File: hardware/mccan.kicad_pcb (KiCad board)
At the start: 4 copper layers, 140 x 100 mm, 237 parts, among them J1 PWR pigtail -> SS1.5 3w, J2 Prog/UART, J3 FL pigtail -> SS1.0 key A / b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, J4 FR pigtail -> SS1.0 key B / g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, J5 RL pigtail -> SS1.0 key C / b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, J6 RR pigtail -> SS1.0 key D / n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, J7 DENALI pigtail -> SS1.5 3w, J8 CAN pigtail -> SS1.0 2w, Q10 IPT008N06NM5LF, Q11 IPT008N06NM5LF, Q12 MMBT3904, Q2 MMBT3904, Q3 MMBT3904, Q4 NX5020UNBKS, Q5 NX5020UNBKS, Q6 NX5020UNBKS, Q7 NX5020UNBKS, Q8 NX5020UNBKS, Q9 NX5020UNBKS, SW1 BOOT, SW2 EN/RESET, U1 LM5164DDA, U10 LTC4380HMS-2, U2 LM5164DDA, U3 LM51571-Q1, U5 ESP32-WROOM-32E-N8, U6 TJA1042T/3, U7 PCA9685PW/Q900, U8 ADG706, U9 BTS7008-2EPA

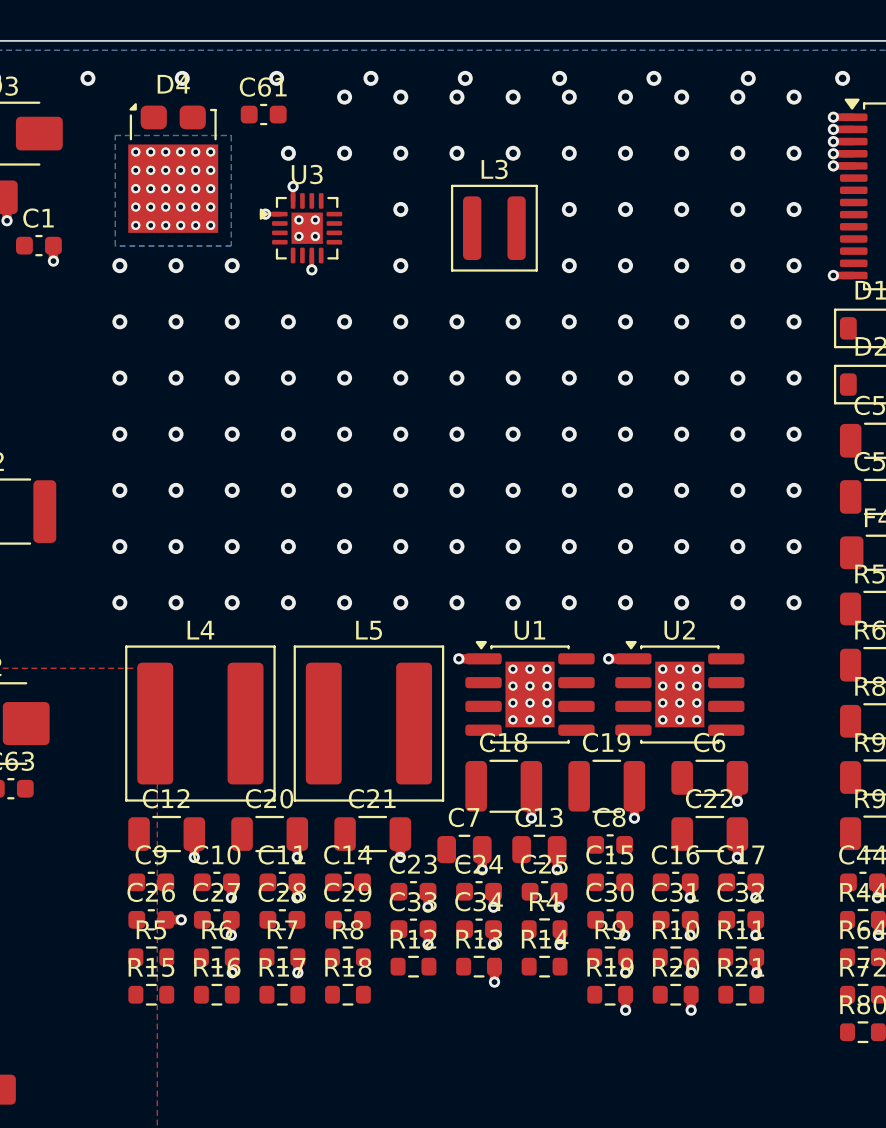
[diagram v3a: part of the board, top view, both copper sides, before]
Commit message: hw(pcb): put the boost's own components next to the boost
U3's entire support network was ~35 mm away, in the `rails` region.  Not because anyone put
it there, but because nobody put it anywhere: layout_pcb.BLOCK pinned only U3, L3, D4 and
C61 to the `boost` region, so every passive fell through to SHEET_REGION and followed its
schematic sheet, which is `rails`.  The region's own comment already said what was meant --
"U3, L3, D4, C61 and their passives" -- and the passives were simply never listed.

What that produced: COMP 35 mm from pin 8, SS 33 mm from pin 10, the FB divider 37 mm from
pin 9, VCC and BIAS with no local bypass at all, and both the input capacitors (C18/C19) and
the output capacitors (C20/C21/C22) roughly 35 mm from the parts they decouple.  COMP is the
error amplifier's output and the highest-impedance node in the converter; a 35 mm run to its
compensation network, past the switch node, is how a boost oscillates.  The switch node
itself spanned 17 mm, which makes a nonsense of "minimise the switch-node loop".

The cluster is now laid out around U3's pinout rather than as a row, because the pinout is
what decides where each network can go: SW on the right and top edges (12, 13, 14), VCC and
BIAS on the left (2, 3), RT/EN/COMP on the bottom (5, 6, 8), FB/SS/MODE on the right
(9, 10, 11).  So the power parts go above and right, the bias network left, the control
network below and right, and nothing has to cross the switch node.

  switch node   17.0 mm -> 5.1 mm span; D4 anode 2.3 mm from U3 pin 14
  FB            37 mm -> a 3.4 mm cluster, R12/C61/R13 in a column with FB facing U3
  COMP          35 mm -> 1.9 mm to R14
  VCC / BIAS    no local bypass -> 2.1 mm and 1.8 mm
  output caps   ~35 mm -> a 1206 column 1.1 mm off D4's cathode tab
  MODE / SS     35 mm -> 5-7 mm; a static level and a slow ramp, so they take the long stubs

VBAT does not need a track to reach L3: In2.Cu is a VBAT plane end to end since ae9319e, so
L3 pad 1 and C18/C19 each re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
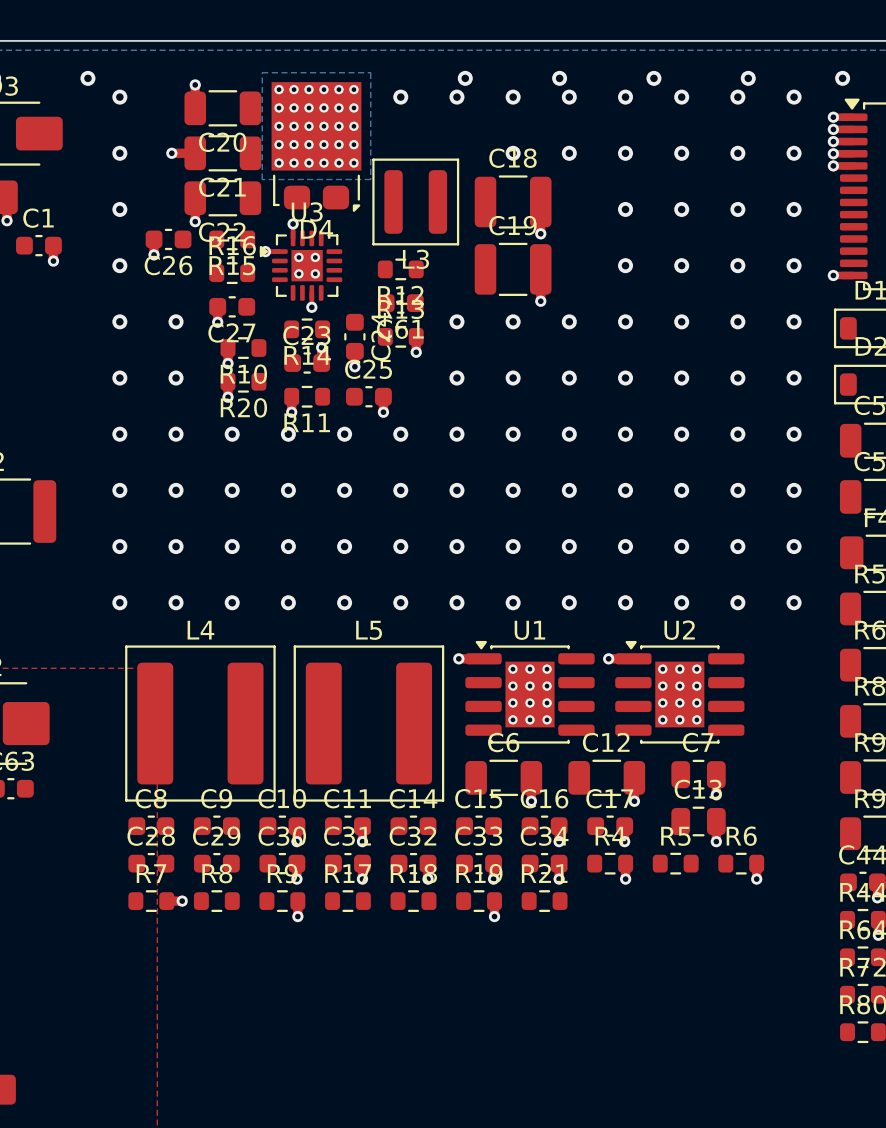
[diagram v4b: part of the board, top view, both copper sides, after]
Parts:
- moved C22 42.8 mm to (69.5, 28.4), turned to 180 degrees
- moved R15 40.6 mm to (70.0, 30.6), turned to 180 degrees
- moved R20 40.0 mm to (70.6, 38.2), turned to 180 degrees
- moved R10 39.9 mm to (70.6, 36.4), turned to 180 degrees
- moved C20 38.8 mm to (69.5, 23.6), turned to 180 degrees
- moved R16 38.5 mm to (70.0, 32.4)
- moved R11 37.9 mm to (74.0, 39.0), turned to 180 degrees
- moved R12 37.2 mm to (79.0, 32.2), turned to 180 degrees
- moved C21 37.2 mm to (69.5, 26.0), turned to 180 degrees
- moved C26 36.3 mm to (66.6, 30.6), turned to 180 degrees
- moved R14 36.3 mm to (74.0, 35.4), turned to 180 degrees
- moved R13 33.9 mm to (79.0, 35.8)
- moved C27 32.7 mm to (70.0, 34.2), turned to 180 degrees
- moved C18 31.2 mm to (85.0, 28.6)
- moved C24 30.4 mm to (76.5, 35.8), turned to 270 degrees
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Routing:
- net GND: vias 331 -> 312

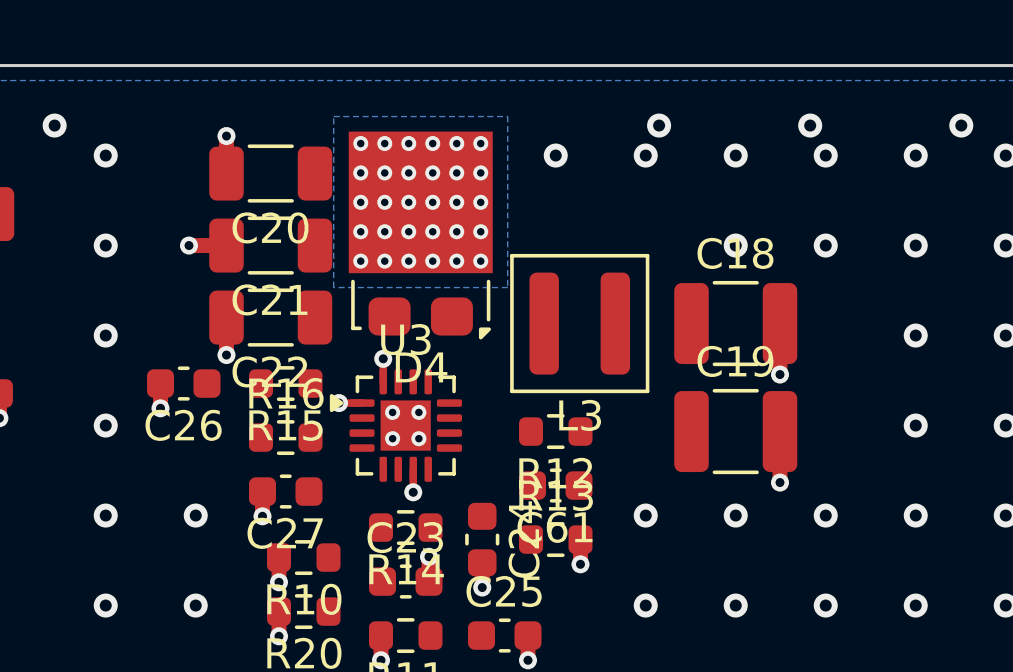
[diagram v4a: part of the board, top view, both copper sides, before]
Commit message: hw(pcb): Task 9 step 1 - route the boost power stage
Adds a route mechanism and uses it for the commutation loop.

layout_pcb.ROUTES is (net, layer, width, [points]) and ROUTE_VIAS is (net, x, y, size,
drill); gen_pcb.routes() emits them and checks two things that are easy to get wrong by hand
and invisible afterwards: that every polyline END lands on copper of its own net, and that
nothing sits closer to a foreign pad than the wider of the two net classes allows.  Both
tests work on COPPER OVERLAP, not on centrelines, because that is what KiCad's connectivity
actually uses -- a 0.75 mm track whose centreline runs between two 0.25 mm QFN pads still
connects to both, and requiring the centreline to hit a pad would rule out the only geometry
that works on a 0.5 mm pitch part.  Nets are named by their last path component, so the
table says "SW_BOOST" and not "/rails/SW_BOOST".

Neither check replaces DRC.  They exist because a coordinate typo produces a board that
looks routed and that DRC can only describe as "unconnected item", somewhere, in a list of
hundreds.  The clearance check earned its keep immediately: the SW track's end cap overlapped
U3's exposed ground paddle, which I had not accounted for because I was thinking about the
endpoint rather than the 0.375 mm of copper past it.

What is routed:

  SW_BOOST   U3 pins 13/14 straight up into D4's anode on one 0.75 mm track, L3 joining from
             the east along y 29.70, and pin 12 tied in at 0.3 mm.  D4 moved 0.8 mm east
             (and L3 and C18/C19 with it) so that D4's anode pad sits directly above pins 13
             and 14: a 0.75 mm track centred between them at x 74.5 overlaps both and still
             clears pin 15 by 0.25 mm.  You cannot bring 0.75 mm of copper into one pin of a
             0.5 mm pitch QFN, but you can bring it into two adjacent pins of the same net,
             and the switch node is worth arranging the placement around to get it.
  +24V       a 1.0 mm column picking up a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
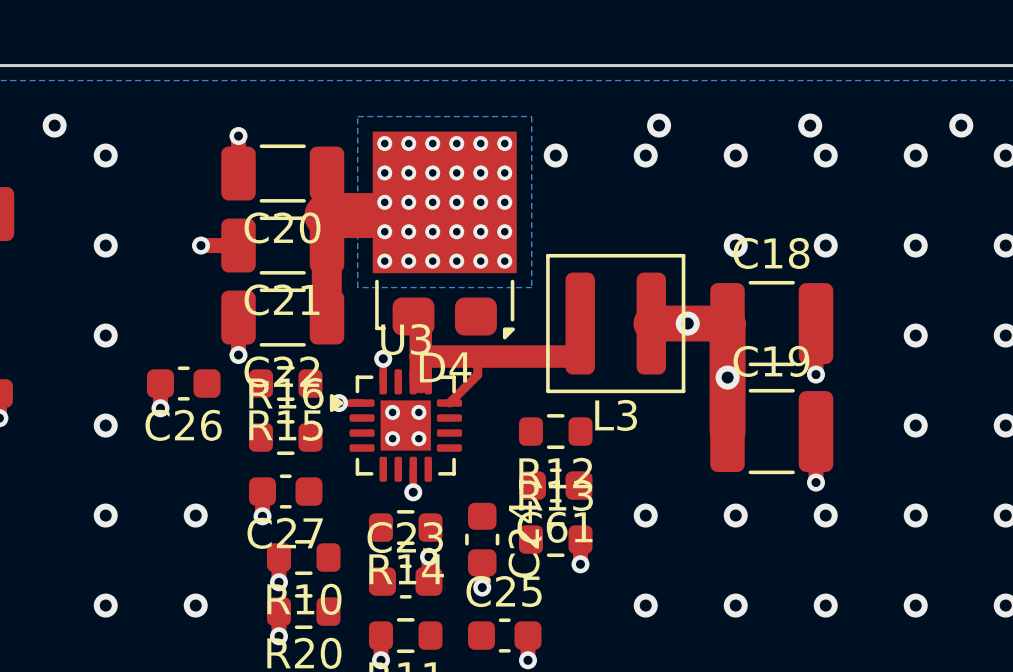
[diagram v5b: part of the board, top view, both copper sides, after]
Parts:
- moved C18 1.20 mm to (86.2, 28.6)
- moved C19 1.20 mm to (86.2, 32.2)
- moved L3 1.20 mm to (81.0, 28.6)
- moved D4 0.80 mm to (75.3, 25.6)
- moved C20 0.40 mm to (69.9, 23.6)
- moved C21 0.40 mm to (69.9, 26.0)
- moved C22 0.40 mm to (69.9, 28.4)
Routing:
- net /rails/SW_BOOST: track 0.00 -> 9.43 mm
- net /+24V: track 0.00 -> 7.03 mm
- net /VBAT: track 0.00 -> 6.14 mm, vias 15 -> 17
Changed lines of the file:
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@@
 	(footprint "Capacitor_SMD:C_1210_3225Metric"
 		(layer "F.Cu")
-		(at 85 28.6)
+		(at 86.2 28.6)
 		(descr "Capacitor SMD 1210 (3225 Metric), square (rectangular) end terminal, IPC-7351 nominal, (Body size source: IPC-SM-782 page 76, https://www.pcb-3d.com/wordpress/wp-content/uploads/ipc-sm-782a_amendment_1_and_2.pdf)")
 		(tags "capacitor")
@@
 	(footprint "Capacitor_SMD:C_1210_3225Metric"
 		(layer "F.Cu")
-		(at 85 32.2)
+		(at 86.2 32.2)
 		(descr "Capacitor SMD 1210 (3225 Metric), square (rectangular) end terminal, IPC-7351 nominal, (Body size source: IPC-SM-782 page 76, https://www.pcb-3d.com/wordpress/wp-content/uploads/ipc-sm-782a_amendment_1_and_2.pdf)")
 		(tags "capacitor")
@@
 	(footprint "Capacitor_SMD:C_1206_3216Metric"
 		(layer "F.Cu")
-		(at 69.5 23.6 180)
+		(at 69.9 23.6 180)
 		(descr "Capacitor SMD 1206 (3216 Metric), square (rectangular) end terminal, IPC-7351 nominal, (Body size source: IPC-SM-782 page 76, https://www.pcb-3d.com/wordpress/wp-content/uploads/ipc-sm-782a_amendment_1_and_2.pdf)")
 		(tags "capacitor")
@@
 	(footprint "Capacitor_SMD:C_1206_3216Metric"
 		(layer "F.Cu")
-		(at 69.5 26 180)
+		(at 69.9 26 180)
 		(descr "Capacitor SMD 1206 (3216 Metric), square (rectangular) end terminal, IPC-7351 nominal, (Body size source: IPC-SM-782 page 76, https://www.pcb-3d.com/wordpress/wp-content/uploads/ipc-sm-782a_amendment_1_and_2.pdf)")
 		(tags "capacitor")
@@
 	(footprint "Capacitor_SMD:C_1206_3216Metric"
 		(layer "F.Cu")
-		(at 69.5 28.4 180)
+		(at 69.9 28.4 180)
 		(descr "Capacitor SMD 1206 (3216 Metric), square (rectangular) end terminal, IPC-7351 nominal, (Body size source: IPC-SM-782 page 76, https://www.pcb-3d.com/wordpress/wp-content/uploads/ipc-sm-782a_amendment_1_and_2.pdf)")
 		(tags "capacitor")
@@
 	(footprint "Package_TO_SOT_SMD:TO-277A"
 		(layer "F.Cu")
-		(at 74.5 25.6 180)
+		(at 75.3 25.6 180)
 		(descr "Thermal enhanced ultra thin SMD package; 3 leads; body: 4.3x6.1x0.43mm, https://www.vishay.com/docs/95570/to-277asmpc.pdf")
 		(tags "TO-277A SMPC")
@@
 	(footprint "Inductor_SMD:L_Coilcraft_XAL4030-XXX"
 		(layer "F.Cu")
-		(at 79.8 28.6 180)
+		(at 81 28.6 180)
 		(descr "Inductor, Coilcraft, XAL4030-XXX, 4.3x4.3x3.1mm, (https://www.coilcraft.com/getmedia/6adcb47d-8b55-416c-976e-1e22e0d2848c/xal4000.pdf)")
 		(tags "xal")
@@
 	)
 	(via
-		(at 76.5 26.52)
+		(at 77.3 26.52)
 		(size 0.5)
 		(drill 0.25)
@@
 	)
 	(via
-		(at 76.5 25.54)
+		(at 77.3 25.54)
 		(size 0.5)
 		(drill 0.25)
@@
 	)
 	(via
-		(at 76.5 24.56)
+		(at 77.3 24.56)
 		(size 0.5)
 		(drill 0.25)
@@
 	)
 	(via
-		(at 76.5 23.58)
+		(at 77.3 23.58)
 		(size 0.5)
 		(drill 0.25)
@@
 	)
 	(via
-		(at 76.5 22.6)
+		(at 77.3 22.6)
 		(size 0.5)
 		(drill 0.25)
@@
 	)
 	(via
-		(at 75.7 26.52)
+		(at 76.5 26.52)
 		(size 0.5)
 		(drill 0.25)
@@
 	)
 	(via
-		(at 75.7 25.54)
+		(at 76.5 25.54)
 		(size 0.5)
 		(drill 0.25)
@@
 	)
 	(via
-		(at 75.7 24.56)
+		(at 76.5 24.56)
 		(size 0.5)
 		(drill 0.25)
@@
 	)
 	(via
-		(at 75.7 23.58)
+		(at 76.5 23.58)
 		(size 0.5)
 		(drill 0.25)
@@
 	)
 	(via
-		(at 75.7 22.6)
+		(at 76.5 22.6)
 		(size 0.5)
 		(drill 0.25)
@@
 	)
 	(via
-		(at 74.9 26.52)
+		(at 75.7 26.52)
 		(size 0.5)
 		(drill 0.25)
@@
 	)
 	(via
-		(at 74.9 25.54)
+		(at 75.7 25.54)
 		(size 0.5)
 		(drill 0.25)
@@
 	)
 	(via
-		(at 74.9 24.56)
+		(at 75.7 24.56)
 		(size 0.5)
 		(drill 0.25)
@@
 	)
 	(via
-		(at 74.9 23.58)
+		(at 75.7 23.58)
 		(size 0.5)
 		(drill 0.25)
@@
 	)
 	(via
-		(at 74.9 22.6)
+		(at 75.7 22.6)
 		(size 0.5)
 		(drill 0.25)
@@
 	)
 	(via
-		(at 74.1 26.52)
+		(at 74.9 26.52)
 		(size 0.5)
 		(drill 0.25)
@@
 	)
 	(via
-		(at 74.1 25.54)
+		(at 74.9 25.54)
 		(size 0.5)
 		(drill 0.25)
@@
 	)
 	(via
-		(at 74.1 24.56)
+		(at 74.9 24.56)
 		(size 0.5)
 		(drill 0.25)
@@
 	)
 	(via
-		(at 74.1 23.58)
+		(at 74.9 23.58)
 		(size 0.5)
 		(drill 0.25)
@@
 	)
 	(via
-		(at 74.1 22.6)
+		(at 74.9 22.6)
 		(size 0.5)
 		(drill 0.25)
@@
 	)
 	(via
-		(at 73.3 26.52)
+		(at 74.1 26.52)
 		(size 0.5)
 		(drill 0.25)
@@
 	)
 	(via
-		(at 73.3 25.54)
+		(at 74.1 25.54)
 		(size 0.5)
 		(drill 0.25)
@@
 	)
 	(via
-		(at 73.3 24.56)
+		(at 74.1 24.56)
 		(size 0.5)
 		(drill 0.25)
@@
 	)
 	(via
-		(at 73.3 23.58)
+		(at 74.1 23.58)
 		(size 0.5)
 		(drill 0.25)
@@
 	)
 	(via
-		(at 73.3 22.6)
+		(at 74.1 22.6)
 		(size 0.5)
 		(drill 0.25)
@@
 	)
 	(via
-		(at 72.5 26.52)
+		(at 73.3 26.52)
 		(size 0.5)
 		(drill 0.25)
@@
 	)
 	(via
-		(at 72.5 25.54)
+		(at 73.3 25.54)
 		(size 0.5)
 		(drill 0.25)
@@
 	)
 	(via
-		(at 72.5 24.56)
+		(at 73.3 24.56)
 		(size 0.5)
 		(drill 0.25)
@@
 	)
 	(via
-		(at 72.5 23.58)
+		(at 73.3 23.58)
 		(size 0.5)
 		(drill 0.25)
@@
 	)
 	(via
-		(at 72.5 22.6)
+		(at 73.3 22.6)
 		(size 0.5)
 		(drill 0.25)
@@
 		(net 106)
 	)
+	(segment
+		(start 74.5 30.55)
+		(end 74.5 28.37)
+		(width 0.75)
+		(layer "F.Cu")
+		(net 105)
+	)
+	(segment
+		(start 79.81 29.7)
+		(end 74.5 29.7)
+		(width 0.75)
+		(layer "F.Cu")
+		(net 105)
+	)
+	(segment
+		(start 75.46 31.25)
+		(end 76.4 30.31)
+		(width 0.3)
+		(layer "F.Cu")
+		(net 105)
+	)
+	(segment
+		(start 76.4 30.31)
+		(end 76.4 29.7)
+		(width 0.3)
+		(layer "F.Cu")
+		(net 105)
+	)
+	(segment
+		(start 71.37 28.4)
+		(end 71.37 23.6)
+		(width 1)
+		(layer "F.Cu")
+		(net 4)
+	)
+	(segment
+		(start 71.37 25)
+		(end 73.6 25)
+		(width 1.5)
+		(layer "F.Cu")
+		(net 4)
+	)
+	(segment
+		(start 82.19 28.6)
+		(end 84.73 28.6)
+		(width 1.2)
+		(layer "F.Cu")
+		(net 22)
+	)
+	(segment
+		(start 84.73 28.6)
+		(end 84.73 32.2)
+		(width 1.2)
+		(layer "F.Cu")
+		(net 22)
+	)
+	(via
+		(at 83.4 28.6)
+		(size 0.8)
+		(drill 0.4)
+		(layers "F.Cu" "B.Cu")
+		(net 22)
+	)
+	(via
+		(at 84.73 30.4)
+		(size 0.8)
+		(drill 0.4)
+		(layers "F.Cu" "B.Cu")
+		(net 22)
+	)
 	(via
 		(at 60.455 31.755)
@@
 	)
 	(via
-		(at 86.475 30.3)
+		(at 87.675 30.3)
 		(size 0.6)
 		(drill 0.3)
@@
 	)
 	(via
-		(at 86.475 33.9)
+		(at 87.675 33.9)
 		(size 0.6)
 		(drill 0.3)
@@
 	)
 	(via
-		(at 68.025 22.35)
+		(at 68.425 22.35)
 		(size 0.6)
 		(drill 0.3)
@@
 	)
 	(via
-		(at 66.775 26)
+		(at 67.175 26)
 		(size 0.6)
 		(drill 0.3)
@@
 	)
 	(via
-		(at 68.025 29.65)
+		(at 68.425 29.65)
 		(size 0.6)
 		(drill 0.3)
@@
 	)
 	(segment
-		(start 86.475 28.6)
-		(end 86.475 30.3)
+		(start 87.675 28.6)
+		(end 87.675 30.3)
 		(width 0.5)
 		(layer "F.Cu")
@@
 	)
 	(segment
-		(start 86.475 32.2)
-		(end 86.475 33.9)
+		(start 87.675 32.2)
+		(end 87.675 33.9)
 		(width 0.5)
 		(layer "F.Cu")
@@
 	)
 	(segment
-		(start 68.025 23.6)
-		(end 68.025 22.35)
+		(start 68.425 23.6)
+		(end 68.425 22.35)
 		(width 0.5)
 		(layer "F.Cu")
@@
 	)
 	(segment
-		(start 68.025 26)
-		(end 66.775 26)
+		(start 68.425 26)
+		(end 67.175 26)
 		(width 0.5)
 		(layer "F.Cu")
@@
 	)
 	(segment
-		(start 68.025 28.4)
-		(end 68.025 29.65)
+		(start 68.425 28.4)
+		(end 68.425 29.65)
 		(width 0.5)
 		(layer "F.Cu")
@@
 		(polygon
 			(pts
-				(xy 71.6 21.7)
-				(xy 77.4 21.7)
-				(xy 77.4 27.4)
-				(xy 71.6 27.4)
+				(xy 72.4 21.7)
+				(xy 78.2 21.7)
+				(xy 78.2 27.4)
+				(xy 72.4 27.4)
 			)
 		)
